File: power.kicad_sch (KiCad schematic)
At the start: 9 parts, among them J401 POWER IN, U401 AMS1117-5.0, U402 AMS1117-3.3

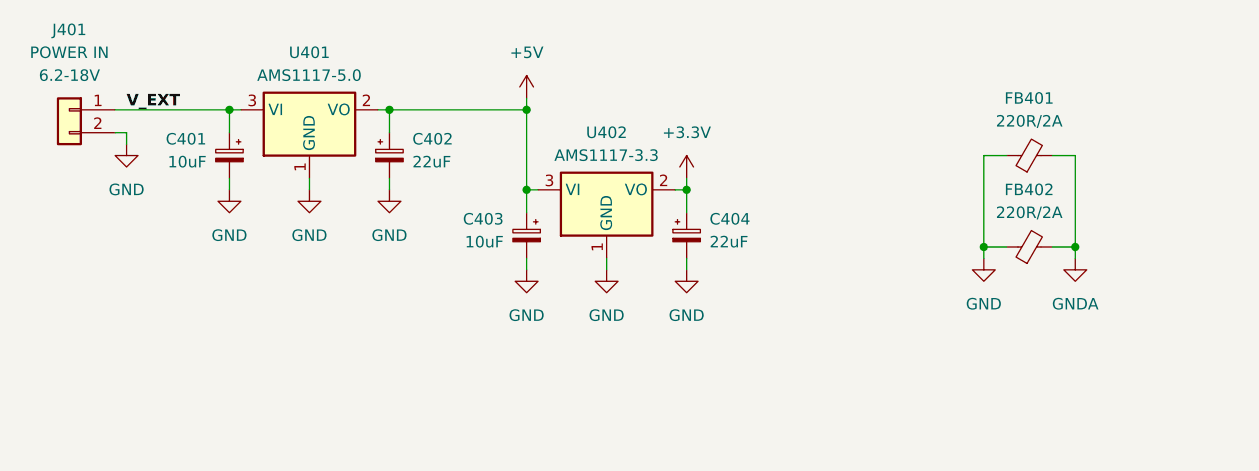
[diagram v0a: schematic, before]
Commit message: Cleaned up schematic
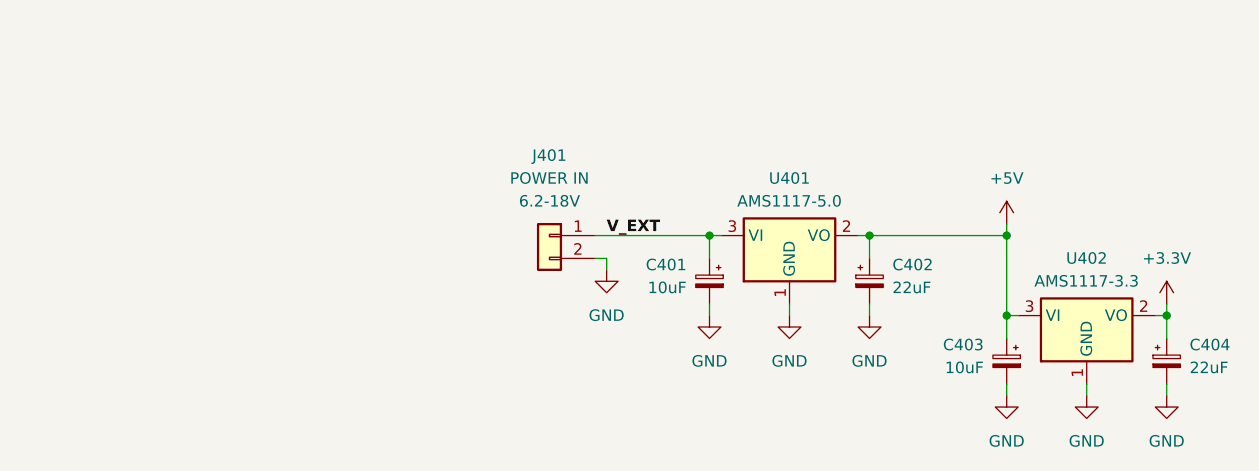
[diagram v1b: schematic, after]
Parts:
- removed FB401, FB402: 220R/2A, Capacitor_SMD:C_0603_1608Metric, symbol Device:FerriteBead_Small
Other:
- moved on the sheet: C401, C402, C403, C404, J401, U401, U402
